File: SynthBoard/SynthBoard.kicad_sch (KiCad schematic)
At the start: 0 parts

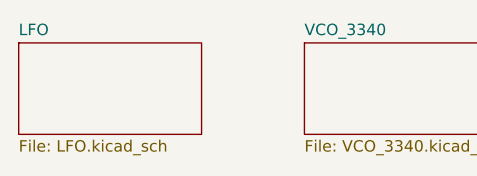
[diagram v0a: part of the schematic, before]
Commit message: SynthBoard
部品をSMDにしてVCO+LFOを配置した
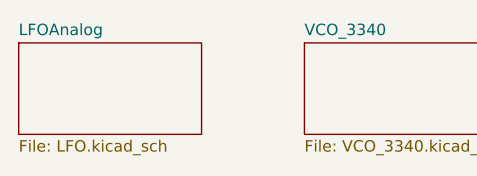
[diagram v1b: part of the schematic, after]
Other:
- sheet LFO renamed LFOAnalog
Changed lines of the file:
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@@
 			(color 0 0 0 0.0000)
 		)
-		(property "Sheetname" "LFO"
+		(property "Sheetname" "LFOAnalog"
 			(at 36.83 25.9584 0)
 			(effects

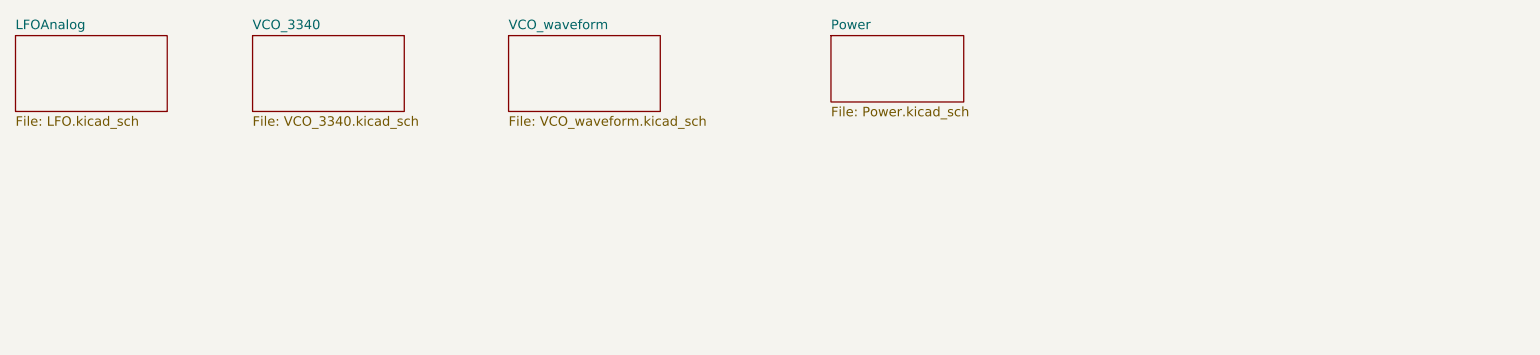
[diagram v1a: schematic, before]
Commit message: SynthBoard
アナログのみ一通り設置 デジタルはなし
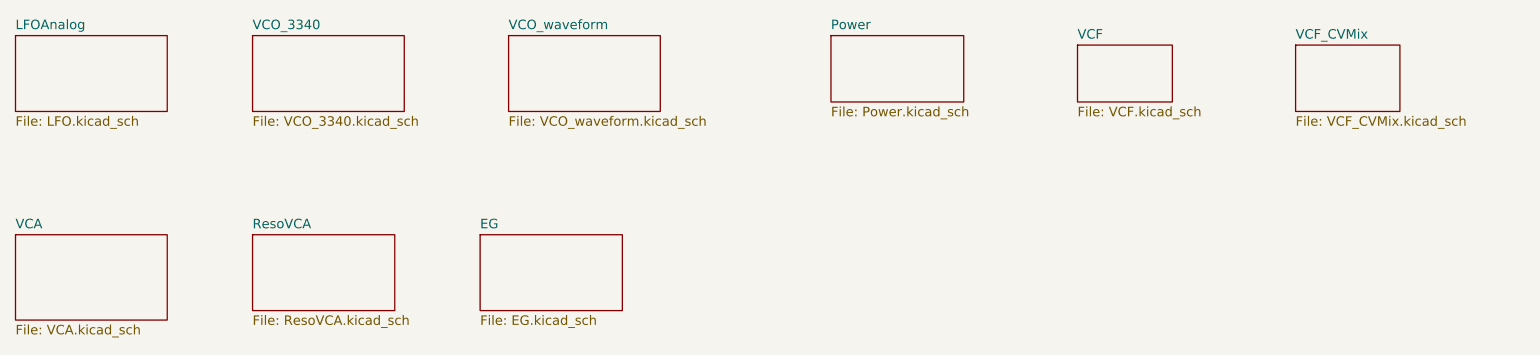
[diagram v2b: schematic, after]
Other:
- added sheet EG (EG.kicad_sch)
- added sheet ResoVCA (ResoVCA.kicad_sch)
- added sheet VCA (VCA.kicad_sch)
- added sheet VCF (VCF.kicad_sch)
- added sheet VCF_CVMix (VCF_CVMix.kicad_sch)
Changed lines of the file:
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@@
+	)
+	(sheet
+		(at 36.83 53.34)
+		(size 20.32 11.43)
+		(exclude_from_sim no)
+		(in_bom yes)
+		(on_board yes)
+		(dnp no)
+		(fields_autoplaced yes)
+		(stroke
+			(width 0.1524)
+			(type solid)
+		)
+		(fill
+			(color 0 0 0 0.0000)
+		)
+		(property "Sheetname" "VCA"
+			(at 36.83 52.6284 0)
+			(effects
+				(font
+					(size 1.27 1.27)
+				)
+				(justify left bottom)
+			)
+		)
+		(property "Sheetfile" "VCA.kicad_sch"
+			(at 36.83 65.3546 0)
+			(effects
+				(font
+					(size 1.27 1.27)
+				)
+				(justify left top)
+			)
+		)
+		(instances
+			(project "SynthBoard"
+				(path "/92765e2f-a998-485f-b610-76a9d5b50cba"
+					(page "8")
+				)
+			)
+		)
+	)
+	(sheet
+		(at 179.07 27.94)
+		(size 12.7 7.62)
+		(exclude_from_sim no)
+		(in_bom yes)
+		(on_board yes)
+		(dnp no)
+		(fields_autoplaced yes)
+		(stroke
+			(width 0.1524)
+			(type solid)
+		)
+		(fill
+			(color 0 0 0 0.0000)
+		)
+		(property "Sheetname" "VCF"
+			(at 179.07 27.2284 0)
+			(effects
+				(font
+					(size 1.27 1.27)
+				)
+				(justify left bottom)
+			)
+		)
+		(property "Sheetfile" "VCF.kicad_sch"
+			(at 179.07 36.1446 0)
+			(effects
+				(font
+					(size 1.27 1.27)
+				)
+				(justify left top)
+			)
+		)
+		(instances
+			(project "SynthBoard"
+				(path "/92765e2f-a998-485f-b610-76a9d5b50cba"
+					(page "6")
+				)
+			)
+		)
 	)
 	(sheet
@@
 	)
 	(sheet
+		(at 208.28 27.94)
+		(size 13.97 8.89)
+		(exclude_from_sim no)
+		(in_bom yes)
+		(on_board yes)
+		(dnp no)
+		(fields_autoplaced yes)
+		(stroke
+			(width 0.1524)
+			(type solid)
+		)
+		(fill
+			(color 0 0 0 0.0000)
+		)
+		(property "Sheetname" "VCF_CVMix"
+			(at 208.28 27.2284 0)
+			(effects
+				(font
+					(size 1.27 1.27)
+				)
+				(justify left bottom)
+			)
+		)
+		(property "Sheetfile" "VCF_CVMix.kicad_sch"
+			(at 208.28 37.4146 0)
+			(effects
+				(font
+					(size 1.27 1.27)
+				)
+				(justify left top)
+			)
+		)
+		(instances
+			(project "SynthBoard"
+				(path "/92765e2f-a998-485f-b610-76a9d5b50cba"
+					(page "7")
+				)
+			)
+		)
+	)
+	(sheet
+		(at 68.58 53.34)
+		(size 19.05 10.16)
+		(exclude_from_sim no)
+		(in_bom yes)
+		(on_board yes)
+		(dnp no)
+		(fields_autoplaced yes)
+		(stroke
+			(width 0.1524)
+			(type solid)
+		)
+		(fill
+			(color 0 0 0 0.0000)
+		)
+		(property "Sheetname" "ResoVCA"
+			(at 68.58 52.6284 0)
+			(effects
+				(font
+					(size 1.27 1.27)
+				)
+				(justify left bottom)
+			)
+		)
+		(property "Sheetfile" "ResoVCA.kicad_sch"
+			(at 68.58 64.0846 0)
+			(effects
+				(font
+					(size 1.27 1.27)
+				)
+				(justify left top)
+			)
+		)
+		(instances
+			(project "SynthBoard"
+				(path "/92765e2f-a998-485f-b610-76a9d5b50cba"
+					(page "9")
+				)
+			)
+		)
+	)
+	(sheet
 		(at 146.05 26.67)
 		(size 17.78 8.89)
@@
 				)
 			)
+		)
+	)
+	(sheet
+		(at 99.06 53.34)
+		(size 19.05 10.16)
+		(exclude_from_sim no)
+		(in_bom yes)
+		(on_board yes)
+		(dnp no)
+		(fields_autoplaced yes)
+		(stroke
+			(width 0.1524)
+			(type solid)
+		)
+		(fill
+			(color 0 0 0 0.0000)
+		)
+		(property "Sheetname" "EG"
+			(at 99.06 52.6284 0)
+			(effects
+				(font
+					(size 1.27 1.27)
+				)
+				(justify left bottom)
+			)
+		)
+		(property "Sheetfile" "EG.kicad_sch"
+			(at 99.06 64.0846 0)
+			(effects
+				(font
+					(size 1.27 1.27)
+				)
+				(justify left top)
+			)
+		)
+		(instances
+			(project "SynthBoard"
+				(path "/92765e2f-a998-485f-b610-76a9d5b50cba"
+					(page "10")
+				)
+			)

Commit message: SynthBorad
デジタルも配置した
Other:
- added sheet Connect (Connect.kicad_sch)
- added sheet LFO Digital (LFO_Digital.kicad_sch)
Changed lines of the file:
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@@
 	(paper "A4")
+	(sheet
+		(at 140.97 54.61)
+		(size 16.51 8.89)
+		(exclude_from_sim no)
+		(in_bom yes)
+		(on_board yes)
+		(dnp no)
+		(fields_autoplaced yes)
+		(stroke
+			(width 0.1524)
+			(type solid)
+		)
+		(fill
+			(color 0 0 0 0.0000)
+		)
+		(property "Sheetname" "LFO Digital"
+			(at 140.97 53.8984 0)
+			(effects
+				(font
+					(size 1.27 1.27)
+				)
+				(justify left bottom)
+			)
+		)
+		(property "Sheetfile" "LFO_Digital.kicad_sch"
+			(at 140.97 64.0846 0)
+			(effects
+				(font
+					(size 1.27 1.27)
+				)
+				(justify left top)
+			)
+		)
+		(instances
+			(project "SynthBoard"
+				(path "/92765e2f-a998-485f-b610-76a9d5b50cba"
+					(page "11")
+				)
+			)
+		)
+	)
 	(sheet
 		(at 68.58 26.67)
@@
 				)
 			)
+		)
+	)
+	(sheet
+		(at 180.34 55.88)
+		(size 15.24 7.62)
+		(exclude_from_sim no)
+		(in_bom yes)
+		(on_board yes)
+		(dnp no)
+		(fields_autoplaced yes)
+		(stroke
+			(width 0.1524)
+			(type solid)
+		)
+		(fill
+			(color 0 0 0 0.0000)
+		)
+		(property "Sheetname" "Connect"
+			(at 180.34 55.1684 0)
+			(effects
+				(font
+					(size 1.27 1.27)
+				)
+				(justify left bottom)
+			)
+		)
+		(property "Sheetfile" "Connect.kicad_sch"
+			(at 180.34 64.0846 0)
+			(effects
+				(font
+					(size 1.27 1.27)
+				)
+				(justify left top)
+			)
+		)
+		(instances
+			(project "SynthBoard"
+				(path "/92765e2f-a998-485f-b610-76a9d5b50cba"
+					(page "12")
+				)
+			)
